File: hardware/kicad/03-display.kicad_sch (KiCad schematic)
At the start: 2 parts, among them J4 FPC-16P-0.5mm

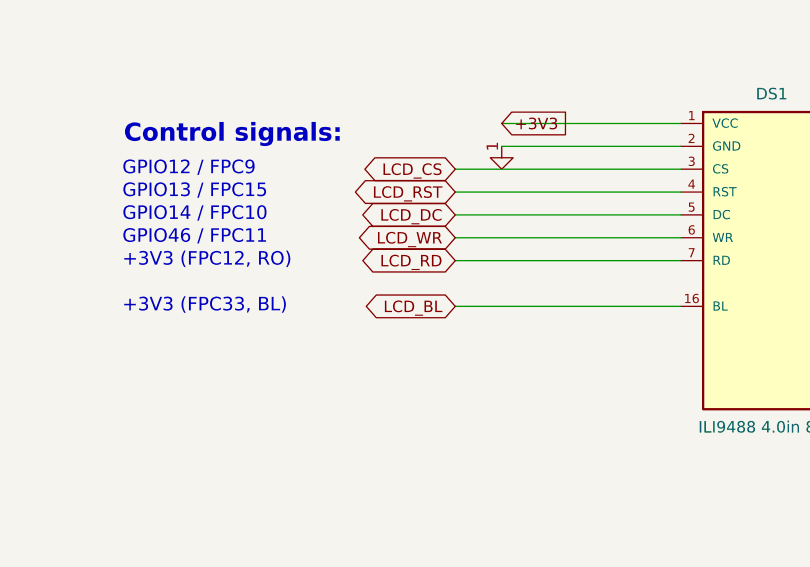
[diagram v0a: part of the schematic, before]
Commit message: cpl+nets: two real rotation bugs, and the release dir that never got U4's fix
The CPL rotation law was red on U2 and J4. Both turned out to be generator
bugs, so this fixes them at the source — `_LAW_EXCEPTIONS` stays an empty
dict and nothing is waived.

U2 (IP5306, C181692, ESOP-8). "ESOP-8" cannot match the `^SOP-` rule in
_JLCPCB_ROT_CORRECTIONS — the anchor is blocked by the leading E — so it
fell through every rule to the 180 default and was emitted at cpl=0. That
is 5.014 mm of lead-to-pad offset on 0.6 mm pads: the part does not touch
its own copper. At 90 it seats pin-for-pin (0.090 mm). Same one-letter miss
that put U4's SOT-23-6 on the SOT-23-3 rule.

J4 (FPC-40P, C2856812). _JLCPCB_ROT_DELTAS["J4"] = 180 was the table's last
live entry and had exactly the defect the table header warns about: an
eyeballed 3D overlay (404f31a), no derivation. The same 270 had already
been removed four days earlier in 2d35646 — "would reverse all 40 FPC
pins!" — which was the correct reading. Both angles solder, since a 180
turn maps a 40-contact single row onto itself; they differ by contact i
landing on pad i versus pad 41-i. A rigid fit of all 42 pads against the
cached reference, numbering preserved, has a unique optimum at the law's
angle (0.004 mm) against 16.55 mm for the alternative.

The 270 was defended by `j4_rot == 270` in verify_dfm_v2 — a tautology that
restated the generator's own output, so when the number was wrong the
assertion defended the bug. It now derives the expected angle from the law.

Not conflated with connector_pad = 41 - panel_pin: that mapping is correct
and untouched.

release_jlcpcb was carrying a stale U4. At HEAD the generator emitted
cpl=0 but release_jlcpcb/cpl.csv still said 90 — the fix closed in 1765982
never reached the directory people actually order from. Re-synced here.

Also drops the phantom nets LCD_RD/LCD_BL (ids 18/19 now retired gaps),
which were the only two DRC warnings. Their FPC pins are tied to +3V3, so
the names carrie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
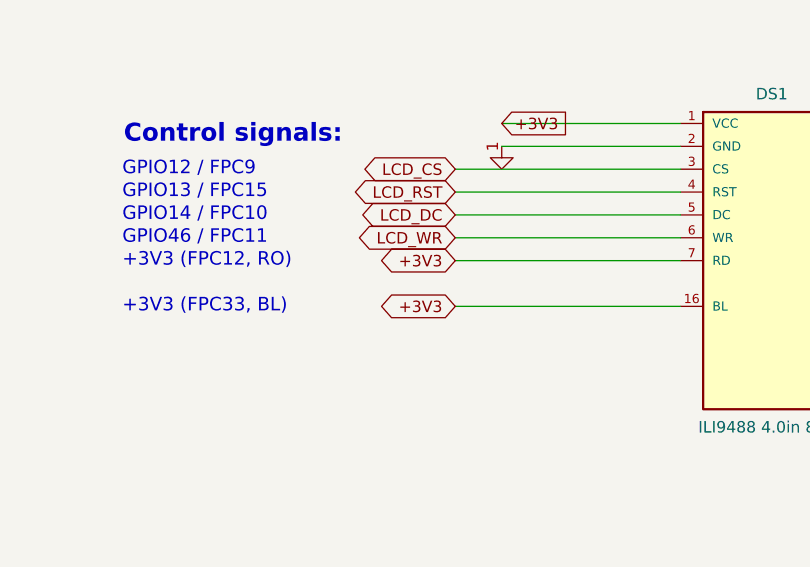
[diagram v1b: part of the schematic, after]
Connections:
- net LCD_BL is gone; now on net +3V3: DS1.16 (BL)
- net LCD_RD is gone; now on net +3V3: DS1.7 (RD)
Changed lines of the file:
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@@
   (text "GPIO46 / FPC11" (at 75.84 117.46 0) (effects (font (size 1.5 1.5)) (justify left)))
   (wire (pts (xy 137.84 120) (xy 112.84 120)) (stroke (width 0) (type default)))
-  (global_label "LCD_RD" (shape bidirectional) (at 112.84 120 180) (effects (font (size 1.27 1.27))) (property "Intersheetrefs" "" (at 0 0 0) (effects (font (size 1.27 1.27)) hide)))
+  (global_label "+3V3" (shape bidirectional) (at 112.84 120 180) (effects (font (size 1.27 1.27))) (property "Intersheetrefs" "" (at 0 0 0) (effects (font (size 1.27 1.27)) hide)))
   (text "+3V3 (FPC12, RO)" (at 75.84 120 0) (effects (font (size 1.5 1.5)) (justify left)))
   (wire (pts (xy 137.84 125.08) (xy 112.84 125.08)) (stroke (width 0) (type default)))
-  (global_label "LCD_BL" (shape bidirectional) (at 112.84 125.08 180) (effects (font (size 1.27 1.27))) (property "Intersheetrefs" "" (at 0 0 0) (effects (font (size 1.27 1.27)) hide)))
+  (global_label "+3V3" (shape bidirectional) (at 112.84 125.08 180) (effects (font (size 1.27 1.27))) (property "Intersheetrefs" "" (at 0 0 0) (effects (font (size 1.27 1.27)) hide)))
   (text "+3V3 (FPC33, BL)" (at 75.84 125.08 0) (effects (font (size 1.5 1.5)) (justify left)))
   (text "8-bit data bus:" (at 173 100 0) (effects (font (size 2 2) bold) (justify left)))

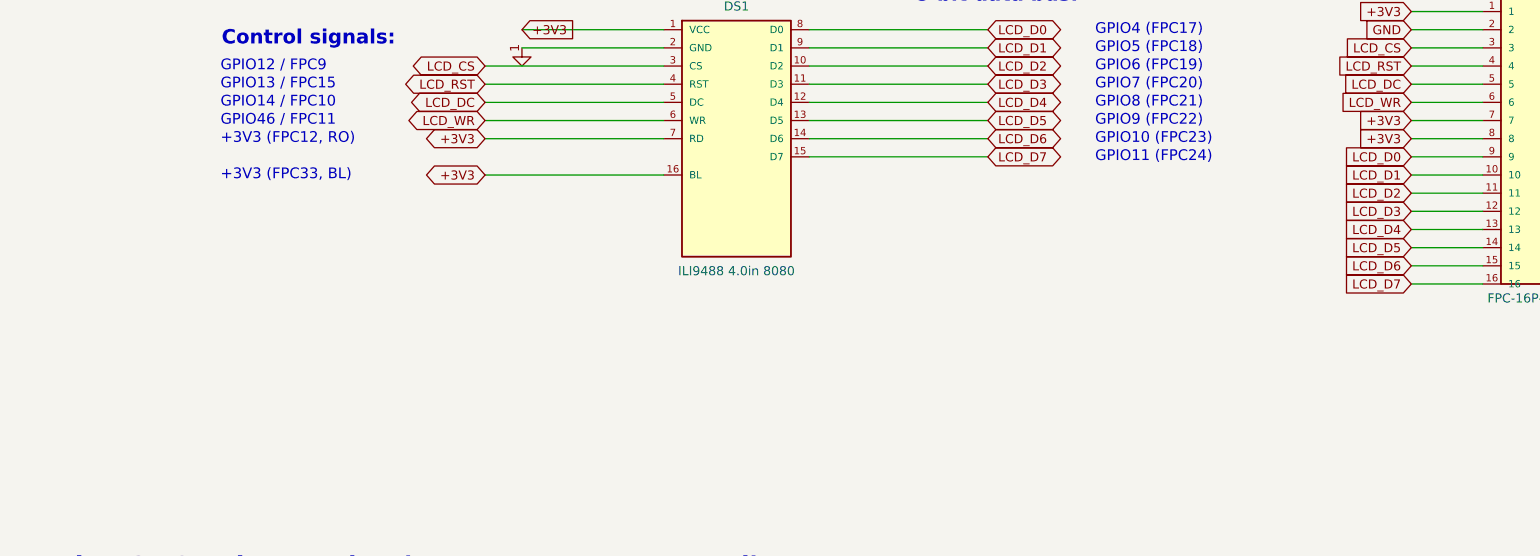
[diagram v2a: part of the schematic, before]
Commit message: feat(hw): EN RC network, fused VBUS input, current-limited backlight — R25 respin trio
Three coordinated design fixes landed together with their full gate,
bench and release integration (work split across two parallel sessions):

- R3 (10k) + C31 (100nF) on EN — the RC the module datasheet p.28
  fig.7 requires (R25-CRIT-1: every board through v4.3.1 shipped
  without it on the strength of a false justification comment).
  EN now solves to the +3V3 rail through the pull-up.
- F1 (PTC resettable fuse 2A 1812, C960026) on the USB input:
  J1 delivers on the new VBUS_IN net and reaches VBUS through F1.
  PWR_FLAG added on the post-fuse rail (J1's power-out pin moved nets).
- R27 (20R 1206) backlight series resistor: LED-A now fed from +5V
  through R27 on the new LED_BLA net (R25-HIGH-1, unbounded current).
  First placement collided with the LCD B.Cu verticals; final position
  (121.7, 45.5) clears the corridor.

Integration completed in this commit:
- verify_polarity: strict expectations for R3/C31/R27/F1, J1 pins moved
  to VBUS_IN, J4.8 backlight expectation moved to LED_BLA — all read
  off the copper.
- vbench corpus: R25-CRIT-1, R10-LOW-7, R25-HIGH-1 flipped from live
  board facts to mutation reinjection (detach R3/C31/R27 must be caught
  by name); R24-HIGH-3 moved to a move_pin drift mutation — the detach
  variant became structurally invisible to the bench once EN gained
  R3/C31 (declared-pad D3 exemption); note records why. usb_cold_boot
  flips its EN assertion exactly as its own text promised; export
  header now derives VB_EN_FLOATING=0; VBUS invariant follows the
  fused chain.
- Gates: R_1206/F_1812 footprints known, F1 value mapping, LED_BLA in
  the Net Explorer section law, schematic caption collisions resolved.
- Release fully synced (gerbers, BOM, CPL, d356, zip, jlcpcb mirror),
  iBOM + schematic SVG/PDF renders + combined PDF regenerated.

Tests: verify-all ALL CHECKS PASSED (incl. polarity 274 checks,
netlist-diff, isolation, e-test on release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
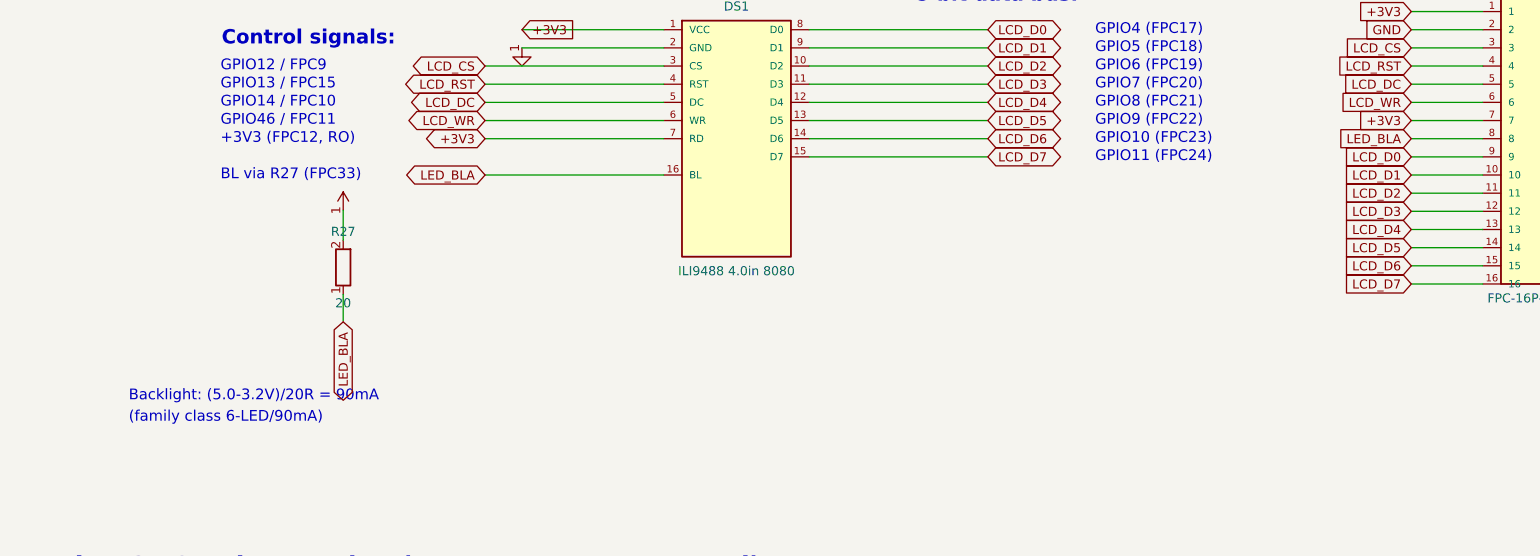
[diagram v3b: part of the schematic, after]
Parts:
- added R27: 20, symbol R
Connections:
- net +3V3: no longer DS1.16 (BL), J4.8
- new net +5V: R27.2
- new net LED_BLA: DS1.16 (BL), J4.8, R27.1
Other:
- note added: "(family class 6-LED/90mA)"
- note added: "BL via R27 (FPC33)"
- note added: "Backlight: (5.0-3.2V)/20R = 90mA"
- note removed: "+3V3 (FPC33, BL)"
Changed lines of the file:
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@@
   (text "+3V3 (FPC12, RO)" (at 75.84 120 0) (effects (font (size 1.5 1.5)) (justify left)))
   (wire (pts (xy 137.84 125.08) (xy 112.84 125.08)) (stroke (width 0) (type default)))
-  (global_label "+3V3" (shape bidirectional) (at 112.84 125.08 180) (effects (font (size 1.27 1.27))) (property "Intersheetrefs" "" (at 0 0 0) (effects (font (size 1.27 1.27)) hide)))
-  (text "+3V3 (FPC33, BL)" (at 75.84 125.08 0) (effects (font (size 1.5 1.5)) (justify left)))
+  (global_label "LED_BLA" (shape bidirectional) (at 112.84 125.08 180) (effects (font (size 1.27 1.27))) (property "Intersheetrefs" "" (at 0 0 0) (effects (font (size 1.27 1.27)) hide)))
+  (text "BL via R27 (FPC33)" (at 75.84 125.08 0) (effects (font (size 1.5 1.5)) (justify left)))
+  (symbol (lib_id "R") (at 93 138 180) (unit 1) (exclude_from_sim no) (in_bom yes) (on_board yes) (dnp no) (property "Reference" "R27" (at 93 133.0 0) (effects (font (size 1.27 1.27)))) (property "Value" "20" (at 93 143.0 0) (effects (font (size 1.27 1.27)))) (pin "1") (pin "2") (instances (project "esp32-emu-turbo" (path "/00000004-cafe-4000-8000-000000000004" (reference "R27") (unit 1)) (path "/00000001-cafe-4000-8000-000000000001/00000004-cafe-4000-8000-000000000004" (reference "R27") (unit 1)))))
+  (symbol (lib_id "+5V") (at 93 130 0) (unit 1) (exclude_from_sim no) (in_bom no) (on_board no) (dnp no) (property "Reference" "#PWR002" (at 93 128 0) (effects (font (size 1.27 1.27)) hide)) (property "Value" "+5V" (at 93 132 0) (effects (font (size 1.27 1.27)) hide)) (pin "1") (instances (project "esp32-emu-turbo" (path "/00000004-cafe-4000-8000-000000000004" (reference "#PWR002") (unit 1)) (path "/00000001-cafe-4000-8000-000000000001/00000004-cafe-4000-8000-000000000004" (reference "#PWR002") (unit 1)))))
+  (wire (pts (xy 93 130) (xy 93 134.19)) (stroke (width 0) (type default)))
+  (wire (pts (xy 93 141.81) (xy 93.0 145.62)) (stroke (width 0) (type default)))
+  (global_label "LED_BLA" (shape bidirectional) (at 93.0 145.62 270) (effects (font (size 1.27 1.27))) (property "Intersheetrefs" "" (at 0 0 0) (effects (font (size 1.27 1.27)) hide)))
+  (text "Backlight: (5.0-3.2V)/20R = 90mA" (at 63 156 0) (effects (font (size 1.5 1.5)) (justify left)))
+  (text "(family class 6-LED/90mA)" (at 63 159 0) (effects (font (size 1.5 1.5)) (justify left)))
   (text "8-bit data bus:" (at 173 100 0) (effects (font (size 2 2) bold) (justify left)))
   (wire (pts (xy 158.16 104.76) (xy 183.16 104.76)) (stroke (width 0) (type default)))
@@
   (global_label "+3V3" (shape input) (at 242.38 117.46 180) (effects (font (size 1.27 1.27))) (property "Intersheetrefs" "" (at 0 0 0) (effects (font (size 1.27 1.27)) hide)))
   (wire (pts (xy 252.38 117.46) (xy 242.38 117.46)) (stroke (width 0) (type default)))
-  (global_label "+3V3" (shape input) (at 242.38 120.0 180) (effects (font (size 1.27 1.27))) (property "Intersheetrefs" "" (at 0 0 0) (effects (font (size 1.27 1.27)) hide)))
+  (global_label "LED_BLA" (shape input) (at 242.38 120.0 180) (effects (font (size 1.27 1.27))) (property "Intersheetrefs" "" (at 0 0 0) (effects (font (size 1.27 1.27)) hide)))
   (wire (pts (xy 252.38 120.0) (xy 242.38 120.0)) (stroke (width 0) (type default)))
   (global_label "LCD_D0" (shape input) (at 242.38 122.53999999999999 180) (effects (font (size 1.27 1.27))) (property "Intersheetrefs" "" (at 0 0 0) (effects (font (size 1.27 1.27)) hide)))

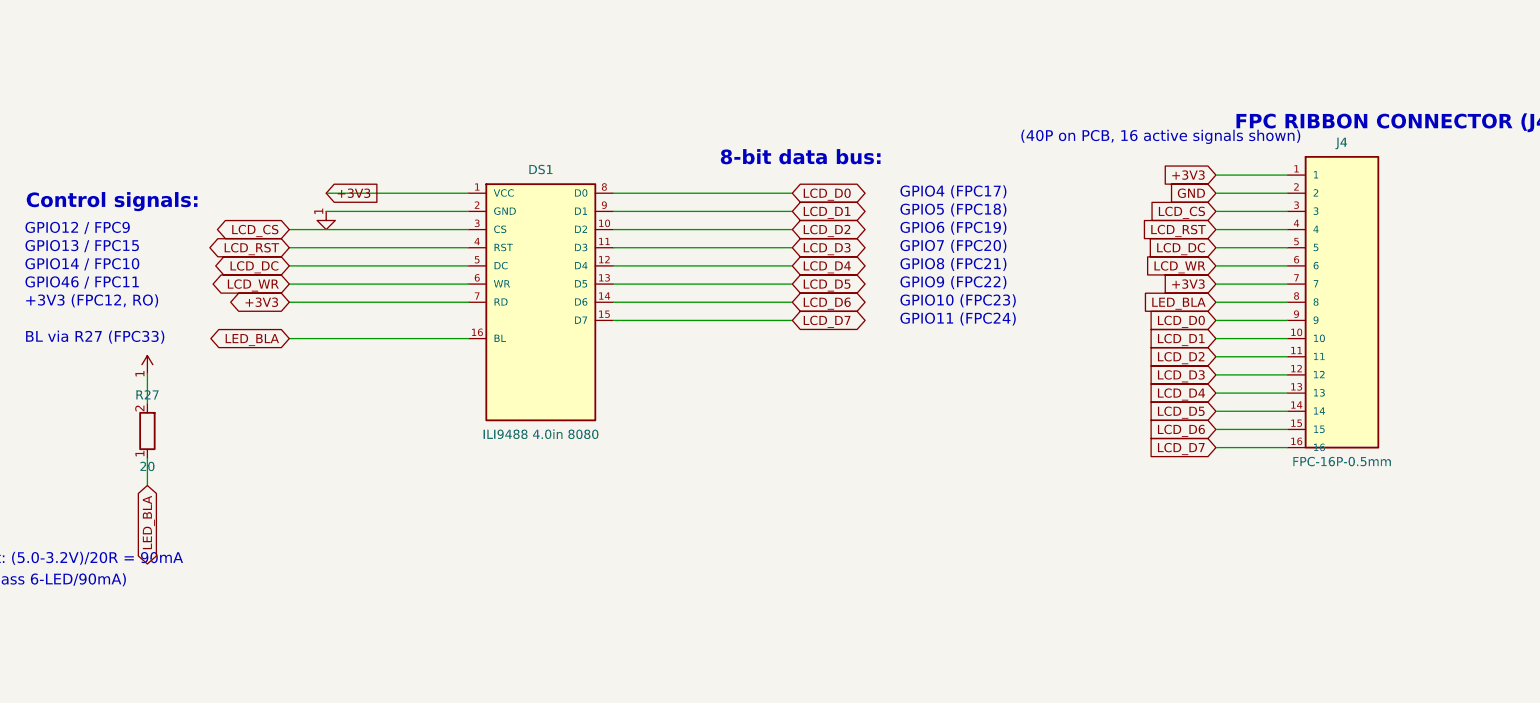
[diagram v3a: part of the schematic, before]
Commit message: feat(containment): layer 6 — ERC warning burn-down, 676 to ZERO, gate at all severities
Three root causes, three fixes in the schematic generator:

- 507 endpoint_off_grid: sheets lay out on a human 1 mm grid while KiCad
  connects on 1.27 mm. snap() in kicad_primitives now grid-snaps every
  connection-bearing coordinate at emission. Snapping is monotonic and
  distributes over the library's grid-multiple pin offsets, so points
  that coincided before still coincide after; zero-length stub wires
  that collapse onto their anchor are dropped.
- The stragglers came from three symbols whose pin connection points
  were themselves off-grid: BAT54C (±5.0 → ±5.08, top 5.0 → 5.08, used
  by D1 and Q1), USBLC6-2SC6 (±10.0 → ±10.16), Speaker (±0.635 →
  ±1.27). Their sheet wiring moved with them in the same commit.
- 169 lib_symbol_issues: bare lib_ids referenced library "" which no
  configuration includes. Symbols are now emu:<name>, resolved by a
  generated hardware/kicad/sym-lib-table + emu.kicad_sym built from the
  same SYMBOLS strings as the embedded caches — cache and library
  cannot disagree by construction.

verify_erc now runs --severity-all against a ZERO baseline: from zero,
any new warning is a regression a specific change introduced. The
website's per-sheet SVGs/PDFs are re-rendered, and the "Download all
sheets" PDF — a one-off hand merge nothing regenerated, stale since the
R25 respin — is now merged by render-schematics.sh from the exported
sheets.

Suite: 85/85 green; netlist_diff vs PCB confirms connectivity unchanged.

Co-Authored-By: Claude Fable 5 <noreply@anthropic.com>
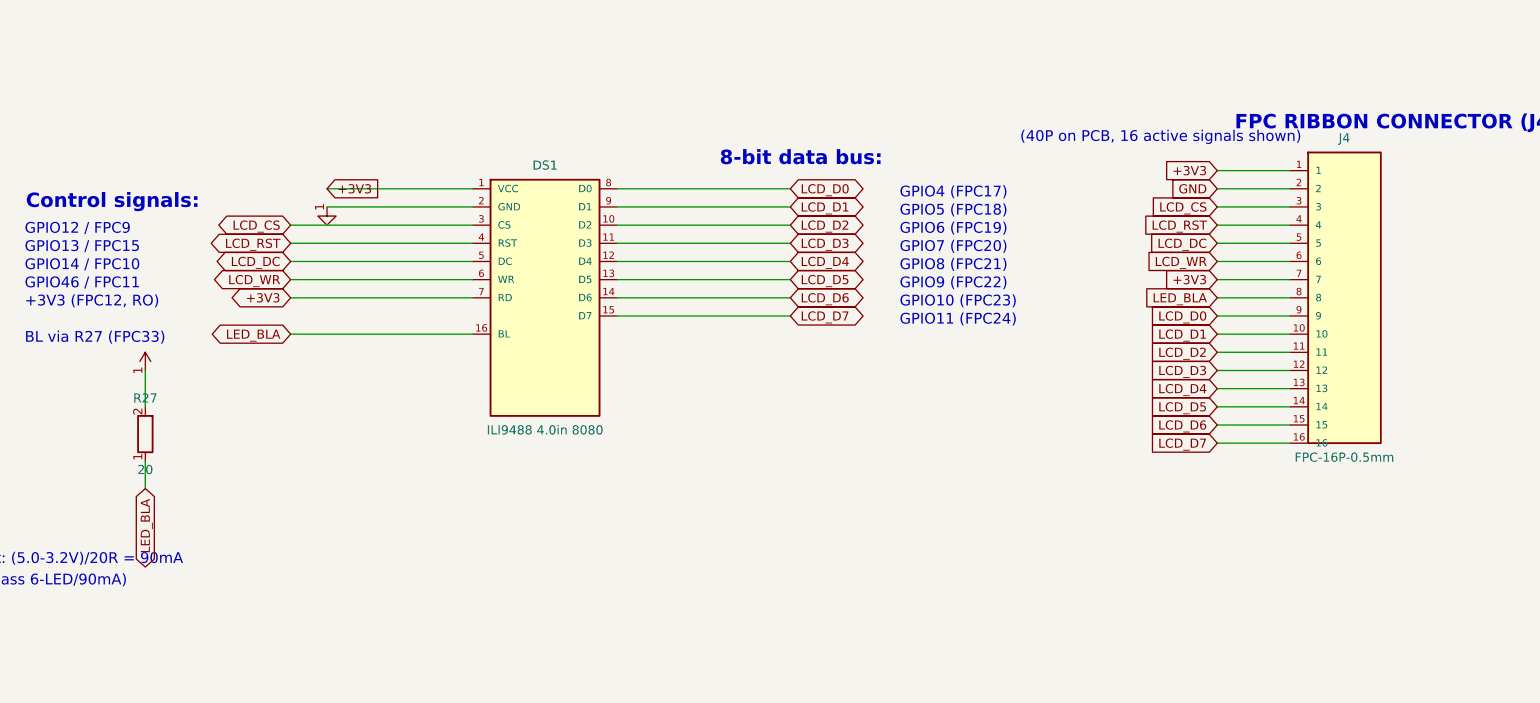
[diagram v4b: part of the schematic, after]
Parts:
- DS1: symbol ST7796S_Module -> emu:ST7796S_Module
- J4: symbol FPC_16P -> emu:FPC_16P
- R27: symbol R -> emu:R
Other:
- moved on the sheet: DS1, J4, R27
